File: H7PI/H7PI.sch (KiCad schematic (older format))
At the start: 52 parts, among them J1 XKTF-015-N, J10 DNP, J2 Header_2x10, J3 microUSB, J4 AFC07-S24ECA-00, J5 Header_2x20, J6 microUSB, J7 Header_1x2, J8 Header_1x1, J9 Header_1x1, Q1 CJ2101, Q2 CJ2102, U2 MT1470, U3 STM32H750VBT6, U4 W25Q64JVSSIQ, U5 W25Q64JVSSIQ

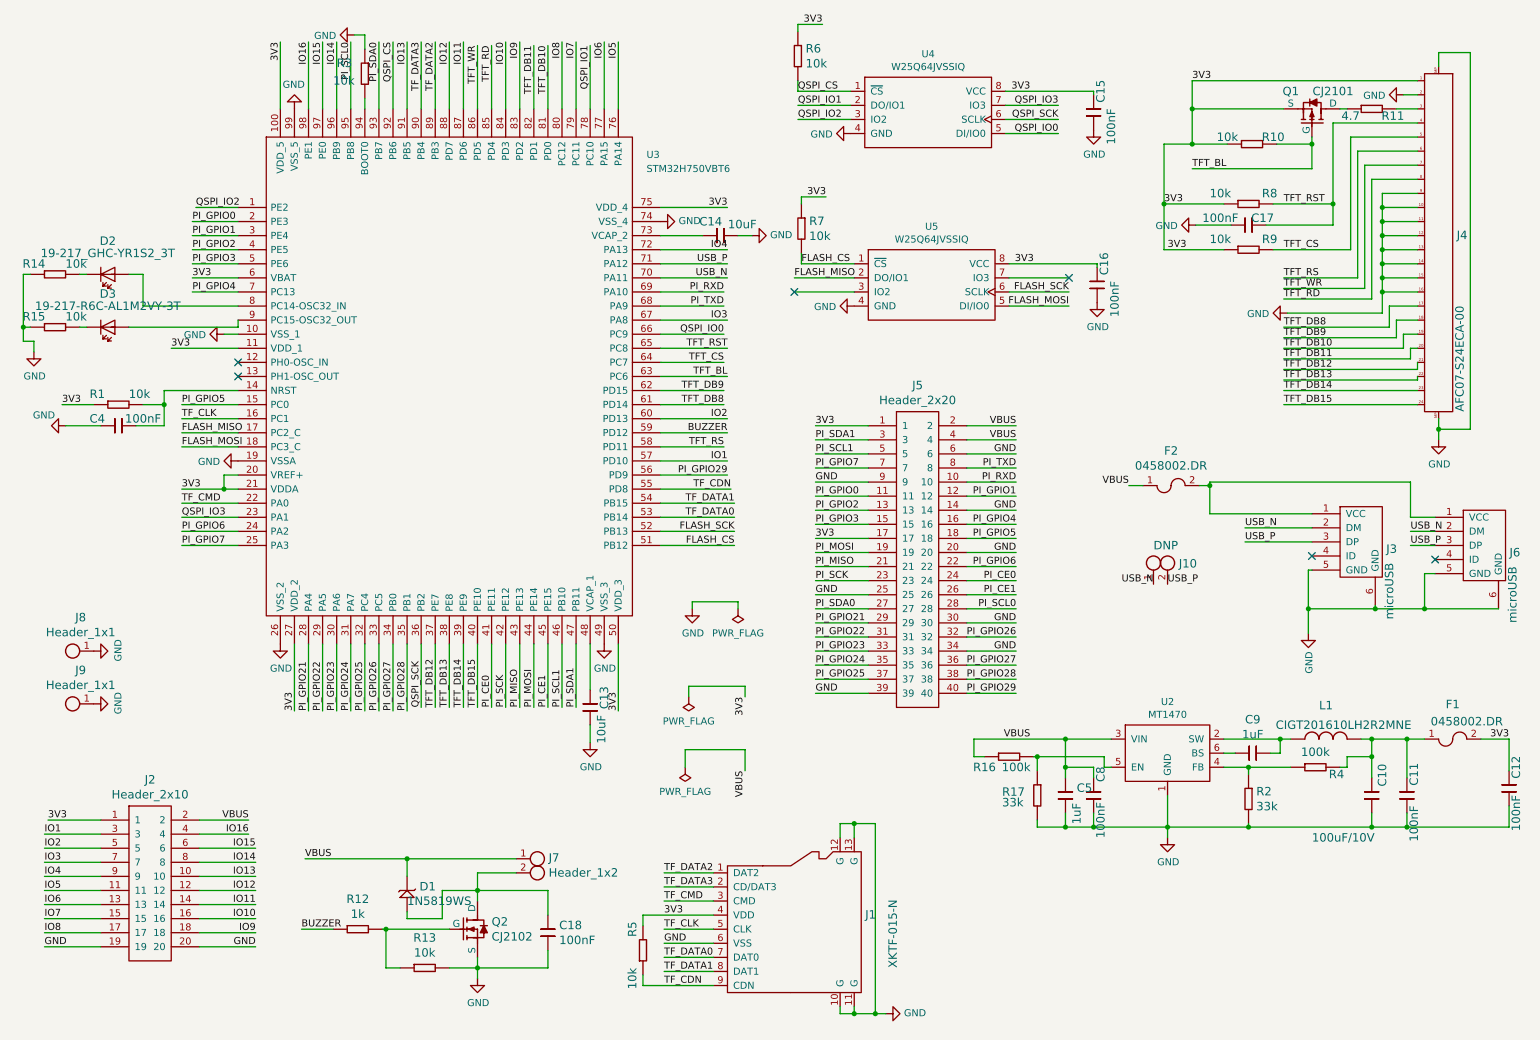
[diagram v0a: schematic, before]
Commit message: v1.0开发起点 1. 不再使用树莓派外型 2. 使用Type C USB接口 3. 不再板载LCD接口 4. 板载PSRAM,QSPI FLASH,SPI FLASH 5. 保留TF卡接口
Signed-off-by: fuhua-chen <fuhua-chen@outlook.com>
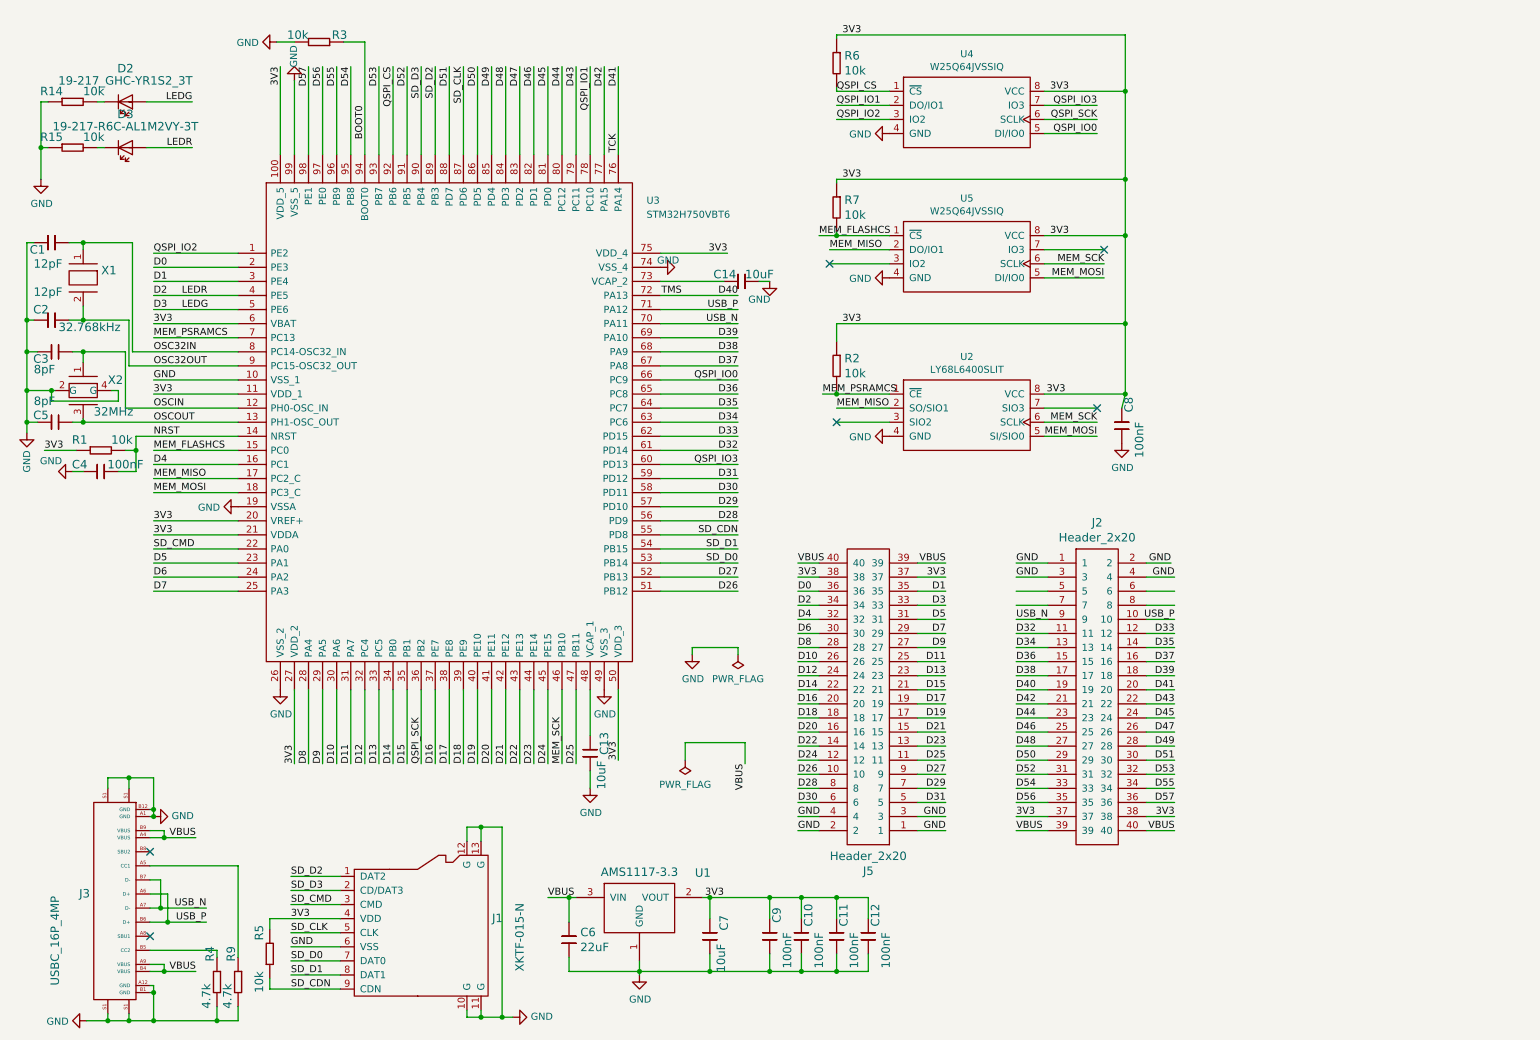
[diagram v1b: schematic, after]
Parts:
- removed C10: 100uF/10V, C_1210_3225Metric, symbol capacitor:CL32A107MPVNNNE
- removed C15, C16, C17, C18: 100nF, C_0402_1005Metric, symbol capacitor:0402B104K500NT
- removed C5, C9: 1uF, C_0603_1608Metric, symbol capacitor:0603B105K500NT
- removed D1: 1N5819WS, D_SOD-323, symbol diode:1N5819WS
- removed F1, F2: 0458002.DR, Fuse_1206_3216Metric, symbol fuse:0458002.DR
- removed J10: DNP, PinHeader_1x02_P2.54mm_Vertical, symbol connector:Header_1x2
- removed J2: Header_2x10, PinHeader_2x10_P2.54mm_Vertical, symbol connector:Header_2x10
- removed J3, J6: microUSB, USB_Micro-B_Molex-105017-0001, symbol connector:microUSB
- removed J4: AFC07-S24ECA-00, Connector_FPC_JS_AFC07-S24ECA-00_1x24-1MP_P0.5mm_UpSideContact, symbol connector:AFC07-S24ECA-00
- removed J7: Header_1x2, Connector_PinHeader_1.27mm:PinHeader_1x02_P1.27mm_Vertical, symbol connector:Header_1x2
- removed J8, J9: Header_1x1, TestPoint:TestPoint_Pad_D1.0mm, symbol connector:Header_1x1
- removed L1: CIGT201610LH2R2MNE, L_0805_2012Metric_Pad1.15x1.40mm_HandSolder, symbol inductor:CIGT201610LH2R2MNE
- removed Q1: CJ2101, SOT-323_SC-70, symbol mosfet:CJ2101
- removed Q2: CJ2102, SOT-323_SC-70, symbol mosfet:CJ2102
- removed R10, R13, R8, R9: 10k, R_0402_1005Metric, symbol resistor:0402WGF1002TCE
- removed R11: 4.7, R_0402_1005Metric, symbol resistor:0402WGF470KTCE
- removed R12: 1k, R_0402_1005Metric, symbol resistor:0402WGF1001TCE
- removed R16, R4: 100k, R_0402_1005Metric, symbol resistor:0402WGF1003TCE
- removed R17, R2: 33k, R_0402_1005Metric, symbol resistor:0402WGF3302TCE
- removed U2: MT1470, SOT-23-6, symbol pmic:MT1470
- added C1, C2: 12pF, C_0402_1005Metric, symbol capacitor:0402CG120J500NT
- added C10, C9: 100nF, C_0402_1005Metric, symbol capacitor:0402B104K500NT
- added C3, C5: 8pF, C_0402_1005Metric, symbol capacitor:0402CG180J500NT
- added C6: 22uF, Capacitor_SMD:C_0805_2012Metric, symbol capacitor:CL21A226MAQNNNE
- added C7: 10uF, C_0402_1005Metric, symbol capacitor:0402X106M6R3NT
- added J2: Header_2x20, PinHeader_2x20_P2.54mm_Vertical, symbol connector:Header_2x20
- added J3: USBC_16P_4MP, USB_C_Receptacle_Palconn_UTC16-G, symbol connector:USBC_16P_4MP
- added R2: 10k, R_0402_1005Metric, symbol resistor:0402WGF1002TCE
- added R4, R9: 4.7k, R_0402_1005Metric, symbol resistor:0402WGF4701TCE
- added U1: AMS1117-3.3, SOT-223, symbol pmic:AMS1117-3.3
- added U2: LY68L6400SLIT, SOIC-8_3.9x4.9mm_P1.27mm, symbol memory:LY68L6400SLIT
- added X1: 32.768kHz, Crystal_SMD_EuroQuartz_EQ161-2Pin_3.2x1.5mm, symbol crystal:SMD31327681252090
- added X2: 32MHz, Crystal:Crystal_SMD_2520-4Pin_2.5x2.0mm, symbol crystal:S2232000082060
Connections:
- net IO2 is gone; now on net QSPI_IO3: U3.60 (PD13)
- net TFT_DB13 is gone; now on net D17: U3.38 (PE8)
- net TFT_DB14 is gone; now on net D18: U3.39 (PE9)
- net 3V3: now also C11.2, C8.2, J5.37, J5.38, C10.2, C7.1, C9.2, J2.37, J2.38, R2.1, U1.2 (VOUT), U2.8 (VCC); no longer J5.1, J5.17
- net GND: now also J5.1, J5.2, J5.3, J5.4, R3.2, C1.1, C10.1, C2.1, C3.1, C5.1, C6.2, C7.2, C9.1, J2.1, J2.2, J2.3, J2.4, J3.A1 (GND), J3.A12 (GND), J3.B1 (GND), J3.B12 (GND), J3.S1, R4.2, R9.2, U1.1 (GND), U2.4 (GND), X2.2 (G), X2.4 (G); no longer J5.14, J5.20, J5.25, J5.30, J5.34, J5.39, J5.6, J5.9, R3.1
- net QSPI_IO3: no longer U3.23 (PA1)
- net USB_N: now also J2.9, J3.A7 (D-), J3.B7 (D-)
- net USB_P: now also J2.10, J3.A6 (D+), J3.B6 (D+)
- net VBUS: now also J5.39, J5.40, C6.1, J2.39, J2.40, J3.A4 (VBUS), J3.A9 (VBUS), J3.B4 (VBUS), J3.B9 (VBUS), U1.3 (VIN); no longer C8.2, J5.2, J5.4
- net OSCIN: now reaches U3.12 (PH0-OSC_IN)
- net OSCIN: now also C3.2, X2.1
- net OSCOUT: now reaches U3.13 (PH1-OSC_OUT)
- net OSCOUT: now also C5.2, X2.3
- net NRST: now reaches C4.1, R1.2, U3.14 (NRST)
- net D3: now reaches D2.2
- net D3: now also J5.33, U3.5 (PE6); no longer U3.8 (PC14-OSC32_IN)
- net D2: now reaches D3.2
- net D2: now also J5.34, U3.4 (PE5); no longer U3.9 (PC15-OSC32_OUT)
- net BOOT0: now reaches U3.94 (BOOT0)
- net BOOT0: now also R3.1; no longer R3.2
- net BUZZER renamed D31
- net D31: now also J5.5
- net FLASH_CS renamed MEM_FLASHCS
- net MEM_FLASHCS: now also U3.15 (PC0); no longer U3.51 (PB12)
- net FLASH_MISO renamed MEM_MISO
- net MEM_MISO: now also U2.2 (SO/SIO1)
- net FLASH_MOSI renamed MEM_MOSI
- net MEM_MOSI: now also U2.5 (SI/SIO0)
- net FLASH_SCK renamed D27
- net D27: now also J5.9; no longer U5.6 (SCLK)
- net IO1 renamed D29
- net D29: now also J5.7
- net IO10 renamed D48
- net D48: now also J2.27
- net IO11 renamed SD_CLK
- net SD_CLK: now also J1.5 (CLK)
- net IO12 renamed D51
- net D51: now also J2.30
- net IO13 renamed D52
- net D52: now also J2.31
- net IO14 renamed D55
- net D55: now also J2.34
- net IO15 renamed D56
- net D56: now also J2.35
- net IO16 renamed D57
- net D57: now also J2.36
- net IO3 renamed D37
- net D37: now also J2.16
- net IO4 renamed D40
- net D40: now also J2.19
- net IO5 renamed D41
- net D41: now also J2.20
- net IO6 renamed D42
- net D42: now also J2.21
- net IO7 renamed D43
- net D43: now also J2.22
- net IO8 renamed D44
- net D44: now also J2.23
- net IO9 renamed D47
- net D47: now also J2.26
- net PI_CE0 renamed D12
- net D12: now also U3.32 (PC4); no longer U3.41 (PE11)
- net PI_CE1 renamed D10
- net D10: now also U3.30 (PA6); no longer U3.45 (PE15)
- net PI_GPIO0 renamed D0
- net D0: now also J5.36; no longer J5.11
- net PI_GPIO1 renamed D1
- net D1: now also J5.35; no longer J5.12
- net PI_GPIO2 renamed D23
- net D23: now also U3.44 (PE14); no longer U3.4 (PE5)
- net PI_GPIO21 renamed D7
- net D7: now also U3.25 (PA3); no longer U3.28 (PA4)
- net PI_GPIO22 renamed D5
- net D5: now also U3.23 (PA1); no longer U3.29 (PA5)
- removed net PI_GPIO23: J5.33, U3.30 (PA6)
- net PI_GPIO24 renamed D11
- net D11: now also J5.25; no longer J5.35
- removed net PI_GPIO25: J5.37, U3.32 (PC4)
- net PI_GPIO26 renamed D13
- net D13: now also J5.23; no longer J5.32
- net PI_GPIO27 renamed D14
- net D14: now also J5.22; no longer J5.36
- net PI_GPIO28 renamed D15
- net D15: now also J5.21; no longer J5.38
- net PI_GPIO29 renamed D28
- net D28: now also J5.8; no longer J5.40
- net PI_GPIO3 renamed D21
- net D21: now also U3.42 (PE12); no longer U3.5 (PE6)
- net PI_GPIO4 renamed D20
- net D20: now also U3.41 (PE11); no longer U3.7 (PC13)
- net PI_GPIO5 renamed D18
- net D18: no longer U3.15 (PC0)
- net PI_GPIO6 renamed D6
- net D6: now also J5.30; no longer J5.22
- removed net PI_GPIO7: J5.7, U3.25 (PA3)
- net PI_MISO renamed D22
- net D22: now also J5.14; no longer J5.21
- net PI_MOSI renamed D17
- net D17: no longer U3.44 (PE14)
- net PI_RXD renamed D26
- net D26: now also U3.51 (PB12); no longer U3.69 (PA10)
- removed net PI_SCK: J5.23, U3.42 (PE12)
- net PI_SCL0 renamed D54
- net D54: now also J2.33; no longer J5.28
- net PI_SCL1 renamed MEM_SCK
- net MEM_SCK: now also U5.6 (SCLK), U2.6 (SCLK); no longer J5.5
- net PI_SDA0 renamed D53
- net D53: now also J2.32; no longer J5.27
- net PI_SDA1 renamed D25
- net D25: now also J5.11; no longer J5.3
- net PI_TXD renamed D38
- net D38: now also J2.17; no longer J5.8
- net TFT_BL renamed D34
- net D34: now also J2.13
- net TFT_CS renamed D35
- net D35: now also J2.14
- net TFT_DB10 renamed D45
- net D45: now also J2.24
- net TFT_DB11 renamed D46
- net D46: now also J2.25
- net TFT_DB12 renamed D16
- net D16: now also J5.20
- net TFT_DB15 renamed D19
- net D19: now also J5.17
- net TFT_DB8 renamed D32
- net D32: now also J2.11
- net TFT_DB9 renamed D33
- net D33: now also J2.12
- net TFT_RD renamed D49
- net D49: now also J2.28
- net TFT_RS renamed D30
- net D30: now also J5.6
- net TFT_RST renamed D36
- net D36: now also J2.15
- net TFT_WR renamed D50
- net D50: now also J2.29
- net TF_CDN renamed SD_CDN
- net TF_CLK renamed D4
- net D4: now also J5.32; no longer J1.5 (CLK)
- net TF_CMD renamed SD_CMD
- net TF_DATA0 renamed SD_D0
- net TF_DATA1 renamed SD_D1
- net TF_DATA2 renamed SD_D2
- net TF_DATA3 renamed SD_D3
- new net: J3.B5 (CC2), R4.1
- new net: J3.A5 (CC1), R9.1
- new net D24: J5.12, U3.45 (PE15)
- new net D39: J2.18, U3.69 (PA10)
- new net D8: J5.28, U3.28 (PA4)
- new net D9: J5.27, U3.29 (PA5)
- new net MEM_PSRAMCS: R2.2, U2.1 (~CE), U3.7 (PC13)
- new net OSC32IN: C1.2, U3.8 (PC14-OSC32_IN), X1.1
- new net OSC32OUT: C2.2, U3.9 (PC15-OSC32_OUT), X1.2
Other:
- moved on the sheet: C13, C14, C4, D2, D3, J1, J5, R1, R14, R15, R3, R5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
